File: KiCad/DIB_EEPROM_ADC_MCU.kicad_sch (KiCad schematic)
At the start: 64 parts, among them IC1 ISO6762FDWR, IC2 ISO6762FDWR, IC3 ADS131M04IPWR, IC4 STM32H503CBT6, IC5 M24C32-DFDW6TP, X1 Edge connector, X2 N.C., Y1 FD0810004, Y2 ABM8-25.000MHZ-D2X-T

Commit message: r4B3 version: OE fixed, new LEDs for remote programming
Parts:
- C10, C11, C27, C3, C4: Mouser 710-885012007040 -> 80-C0603C102K5R7040
- C18, C21: DigiKey 1276-2723-1-ND -> 1276-3138-1-ND; Mouser 80-C1206C225M5RECLR -> 187-CL31B225KCHSNNE; TME CL31B225KBHNNNE -> C3216X7S2A225KAB
- C22, C23: value 18p -> 10p
- R2, R3, R4, R5, R6, R7, R8, R9: Mouser 603-RC0603FR-10100RL -> 603-RT0603FRE07100RL
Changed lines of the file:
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@@
 	(title_block
 		(title "${project_name}")
-		(date "2025-10-23")
+		(date "2025-11-21")
 		(rev "${project_version}")
 		(company "${project_creator}")
@@
 			)
 		)
-		(property "Mouser" "603-RC0603FR-10100RL"
+		(property "Mouser" "603-RT0603FRE07100RL"
 			(at 127 139.7 90)
 			(effects
@@
 			)
 		)
-		(property "Mouser" "710-885012007040 "
+		(property "Mouser" "80-C0603C102K5R7040"
 			(at 71.12 134.62 0)
 			(effects
@@
 			)
 		)
-		(property "Mouser" "603-RC0603FR-10100RL"
+		(property "Mouser" "603-RT0603FRE07100RL"
 			(at 127 116.84 90)
 			(effects
@@
 			)
 		)
-		(property "Mouser" "603-RC0603FR-10100RL"
+		(property "Mouser" "603-RT0603FRE07100RL"
 			(at 63.5 139.7 90)
 			(effects
@@
 			)
 		)
-		(property "Mouser" "603-RC0603FR-10100RL"
+		(property "Mouser" "603-RT0603FRE07100RL"
 			(at 127 132.08 90)
 			(effects
@@
 			)
 		)
-		(property "Value" "18p"
+		(property "Value" "10p"
 			(at 251.079 91.059 90)
 			(effects
@@
 			)
 		)
-		(property "Mouser" "710-885012007040 "
+		(property "Mouser" "80-C0603C102K5R7040"
 			(at 71.12 121.92 0)
 			(effects
@@
 			)
 		)
-		(property "Mouser" "603-RC0603FR-10100RL"
+		(property "Mouser" "603-RT0603FRE07100RL"
 			(at 63.5 124.46 90)
 			(effects
@@
 			)
 		)
-		(property "Mouser" "710-885012007040 "
+		(property "Mouser" "80-C0603C102K5R7040"
 			(at 134.62 137.16 0)
 			(effects
@@
 			)
 		)
-		(property "Mouser" "603-RC0603FR-10100RL"
+		(property "Mouser" "603-RT0603FRE07100RL"
 			(at 63.5 132.08 90)
 			(effects
@@
 			)
 		)
-		(property "Mouser" "603-RC0603FR-10100RL"
+		(property "Mouser" "603-RT0603FRE07100RL"
 			(at 127 124.46 90)
 			(effects
@@
 			)
 		)
-		(property "DigiKey" "1276-2723-1-ND "
+		(property "DigiKey" "1276-3138-1-ND"
 			(at 241.3 147.32 0)
 			(effects
@@
 			)
 		)
-		(property "Mouser" "80-C1206C225M5RECLR"
+		(property "Mouser" "187-CL31B225KCHSNNE"
 			(at 241.3 147.32 0)
 			(effects
@@
 			)
 		)
-		(property "TME" "CL31B225KBHNNNE"
+		(property "TME" "C3216X7S2A225KAB"
 			(at 241.3 147.32 0)
 			(effects
@@
 			)
 		)
-		(property "Mouser" "710-885012007040 "
+		(property "Mouser" "80-C0603C102K5R7040"
 			(at 134.62 121.92 0)
 			(effects
@@
 			)
 		)
-		(property "DigiKey" "1276-2723-1-ND "
+		(property "DigiKey" "1276-3138-1-ND"
 			(at 246.38 147.32 0)
 			(effects
@@
 			)
 		)
-		(property "Mouser" "80-C1206C225M5RECLR"
+		(property "Mouser" "187-CL31B225KCHSNNE"
 			(at 246.38 147.32 0)
 			(effects
@@
 			)
 		)
-		(property "TME" "CL31B225KBHNNNE"
+		(property "TME" "C3216X7S2A225KAB"
 			(at 246.38 147.32 0)
 			(effects
@@
 			)
 		)
-		(property "Value" "18p"
+		(property "Value" "10p"
 			(at 251.079 101.219 90)
 			(effects
@@
 			)
 		)
-		(property "Mouser" "710-885012007040 "
+		(property "Mouser" "80-C0603C102K5R7040"
 			(at 261.62 78.74 0)
 			(effects
@@
 			)
 		)
-		(property "Mouser" "603-RC0603FR-10100RL"
+		(property "Mouser" "603-RT0603FRE07100RL"
 			(at 63.5 116.84 90)
 			(effects

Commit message: Front mask gerbers and dxf update
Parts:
- C22, C23: value 10p -> 30p; DigiKey (none) -> 1292-1515-1-ND; LCSC (none) -> C123555; Mouser (none) -> 80-C0603C300G5HACTU; TME (none) -> 0603N300J500CT
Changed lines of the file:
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@@
 	(title_block
 		(title "${project_name}")
-		(date "2025-11-21")
+		(date "2025-11-22")
 		(rev "${project_version}")
 		(company "${project_creator}")
@@
 			)
 		)
-		(property "Value" "10p"
+		(property "Value" "30p"
 			(at 251.079 91.059 90)
 			(effects
@@
 			)
 		)
-		(property "DigiKey" ""
+		(property "DigiKey" "1292-1515-1-ND"
 			(at 251.46 88.9 0)
 			(effects
@@
 			)
 		)
-		(property "Mouser" ""
+		(property "Mouser" "80-C0603C300G5HACTU"
 			(at 251.46 88.9 0)
 			(effects
@@
 			)
 		)
-		(property "TME" ""
+		(property "TME" "0603N300J500CT"
 			(at 251.46 88.9 0)
 			(effects
@@
 			)
 		)
-		(property "LCSC" ""
+		(property "LCSC" "C123555"
 			(at 251.46 88.9 0)
 			(effects
@@
 			)
 		)
-		(property "Value" "10p"
+		(property "Value" "30p"
 			(at 251.079 101.219 90)
 			(effects
@@
 			)
 		)
-		(property "DigiKey" ""
+		(property "DigiKey" "1292-1515-1-ND"
 			(at 251.46 99.06 0)
 			(effects
@@
 			)
 		)
-		(property "Mouser" ""
+		(property "Mouser" "80-C0603C300G5HACTU"
 			(at 251.46 99.06 0)
 			(effects
@@
 			)
 		)
-		(property "TME" ""
+		(property "TME" "0603N300J500CT"
 			(at 251.46 99.06 0)
 			(effects
@@
 			)
 		)
-		(property "LCSC" ""
+		(property "LCSC" "C123555"
 			(at 251.46 99.06 0)
 			(effects

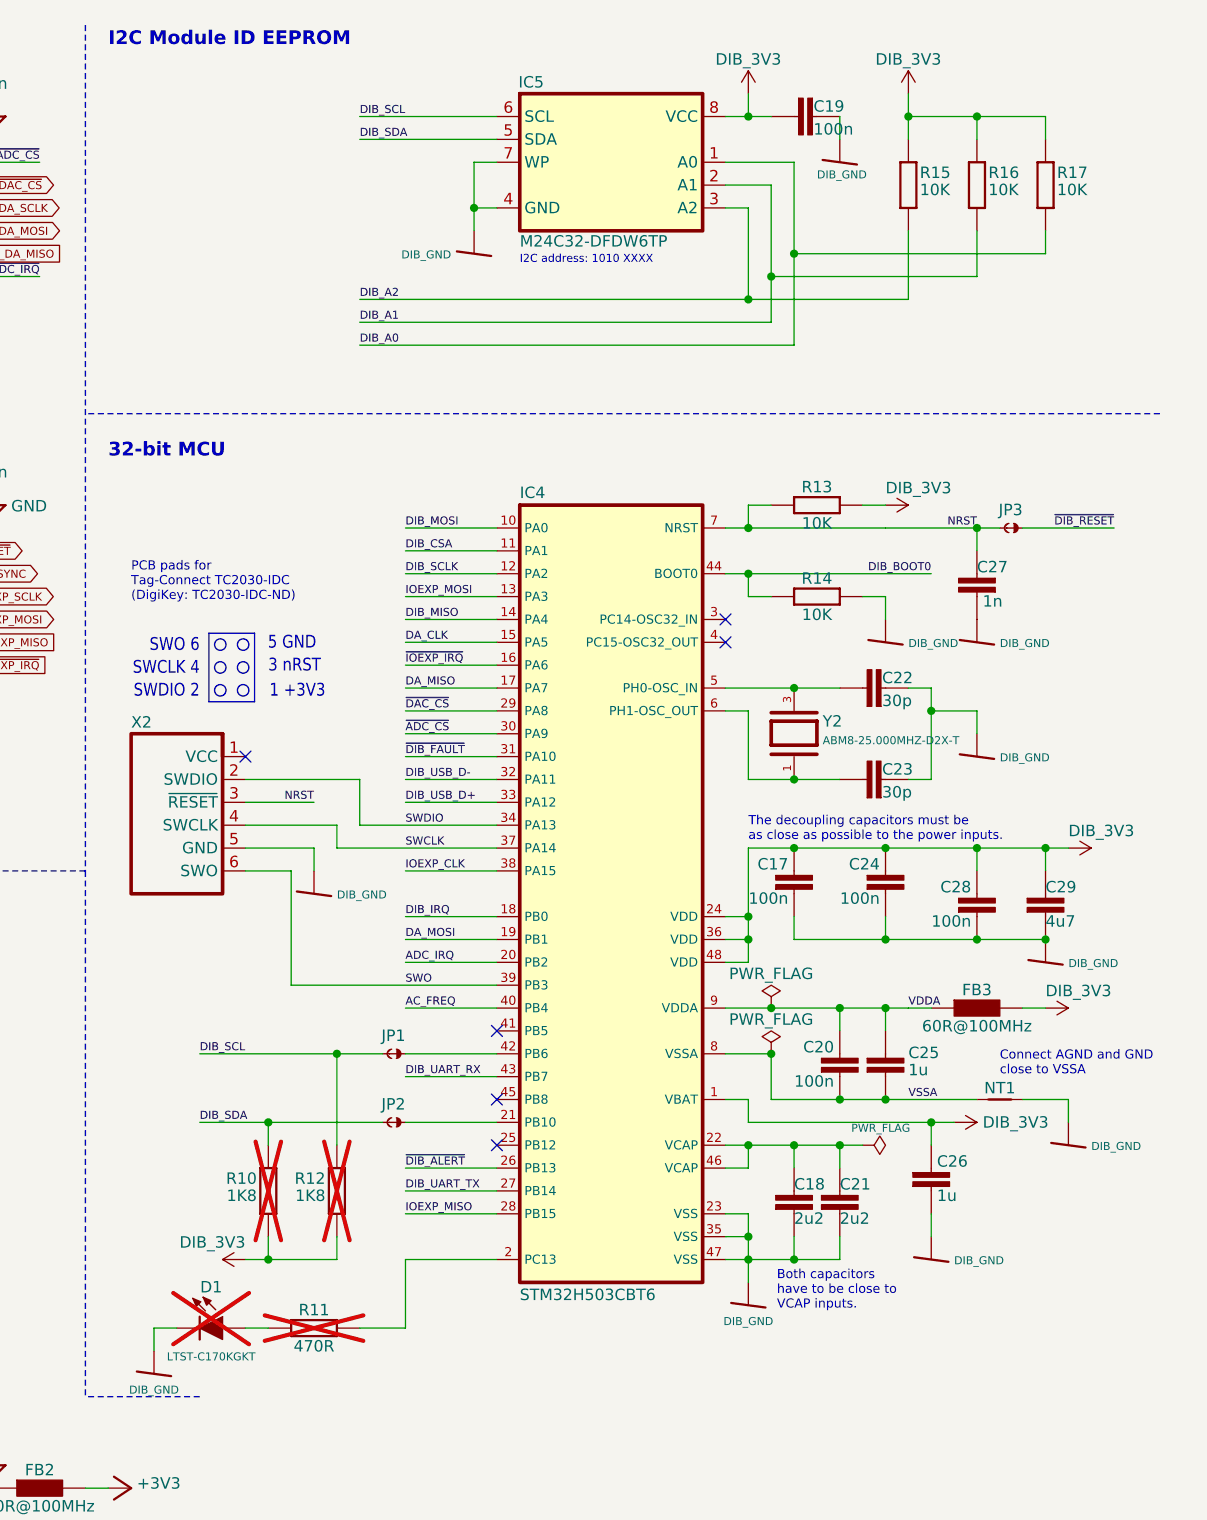
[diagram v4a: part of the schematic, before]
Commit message: EEPROM connected to H503 I2C bus
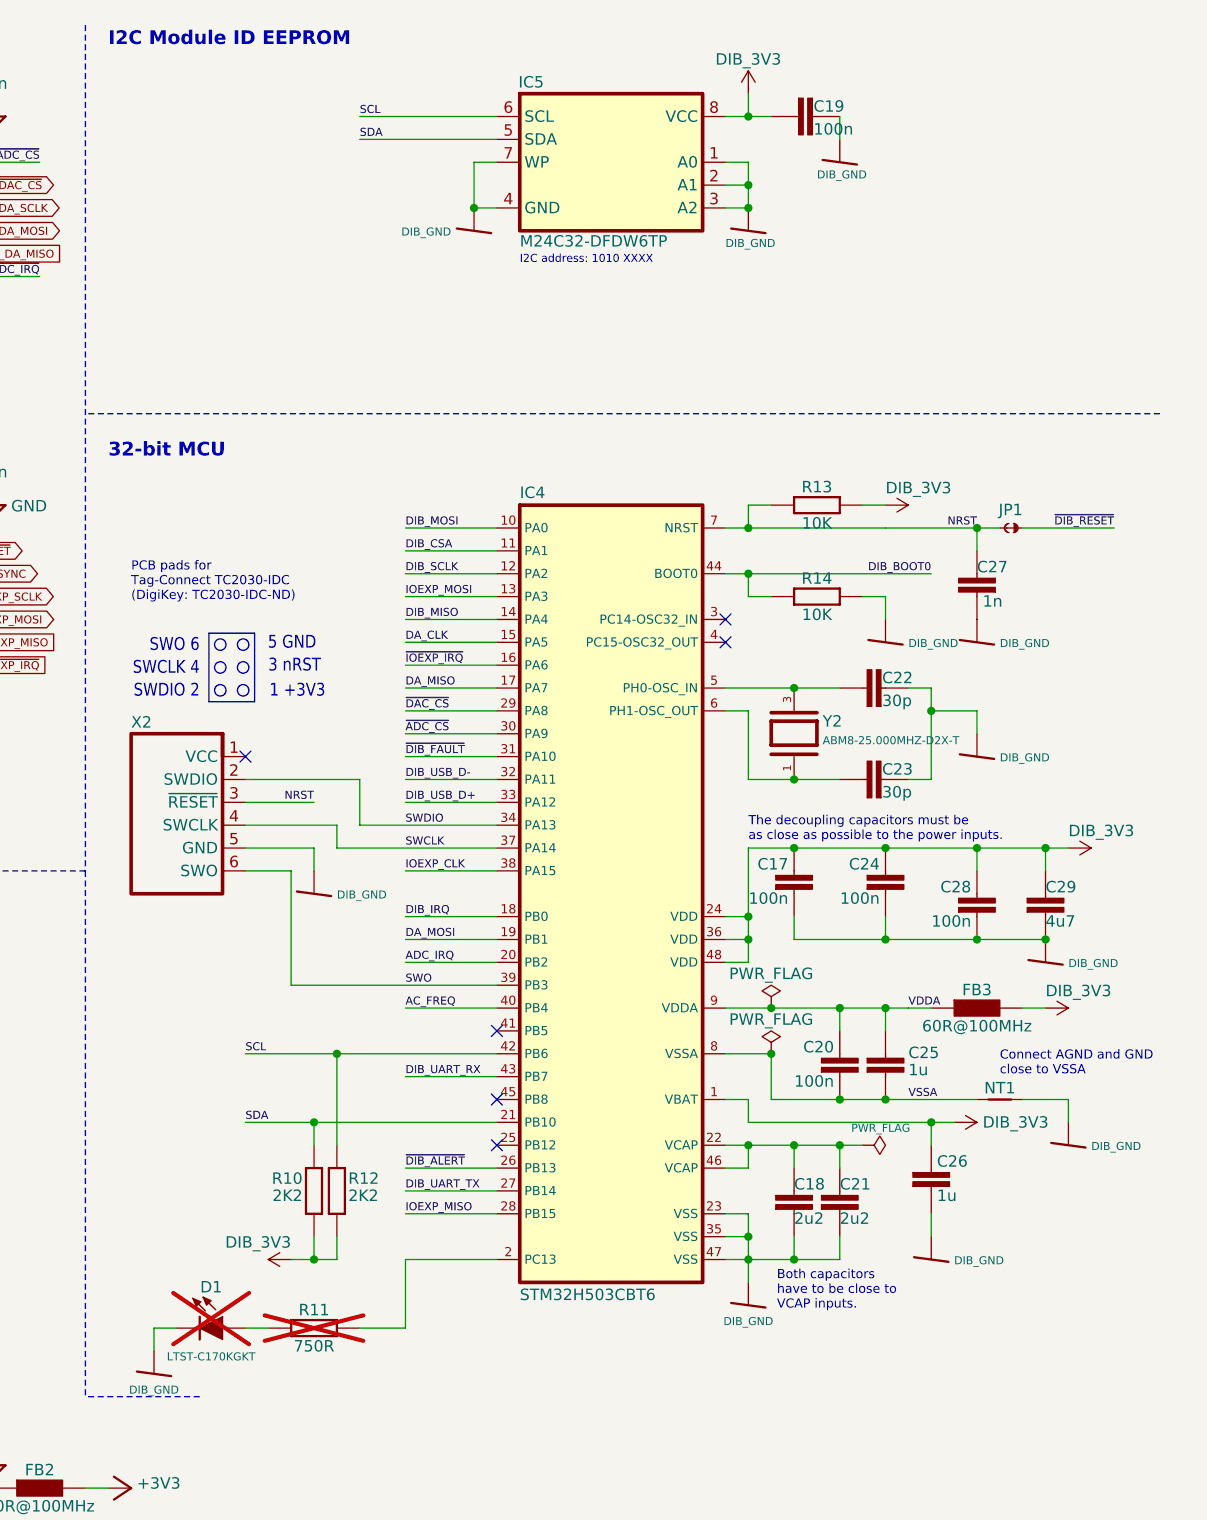
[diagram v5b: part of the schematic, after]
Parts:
- removed JP1, JP2: ~, PCM_EEZ_SMD:JP2 shorted (0603), symbol PCM_EEZ_unsorted:JP2 shorted
- removed R15, R16, R17: 10K, PCM_EEZ_passives:R_0805_2012Metric, symbol PCM_EEZ_passives:R-EU
- R10, R12: value 1K8 -> 2K2; DigiKey (none) -> 311-2.20KCRCT-ND; Mouser (none) -> 603-RC0805FR-072K2L; TME (none) -> 0805S8F2201T5E; now fitted; now in the parts list
- R11: value 470R -> 750R; DigiKey 311-470CRCT-ND -> A126385CT-ND; LCSC (none) -> C17818; Mouser 71-CRCW0805470RFKEB -> 71-CRCW0805750RFKEAC; TME RC0805FR-07470R -> 0805S8F7500T5E
- renumbered JP3 to JP1
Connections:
- net DIB_A0: no longer IC5.1 (A0)
- net DIB_A1: no longer IC5.2 (A1)
- net DIB_A2: no longer IC5.3 (A2)
- net DIB_GND: now also IC5.1 (A0), IC5.2 (A1), IC5.3 (A2)
- net DIB_SCL: no longer IC5.6 (SCL), R12.2
- net DIB_SDA: no longer IC5.5 (SDA), R10.2
- net SDA: now reaches IC4.21 (PB10)
- net SDA: now also IC5.5 (SDA), R10.2
- net SCL: now reaches IC4.42 (PB6)
- net SCL: now also IC5.6 (SCL), R12.2
